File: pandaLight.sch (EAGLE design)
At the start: 161 parts, among them J1 PJ-037A, U1 MIC23450AAAYML, U10 AS4C128M16D3, U11 PMOD-2X6, U12 PMOD-2X6, U13 PLR135-T10, U14 PLT133-T10W, U15 PLR135-T10, U16 TP10SQ, U17 TP10SQ, U18 PAN1322, U2 6SLX45CSG324, U3 TPD4S014SON, U4 FT2232HL, U5 93LC46BT-I/OT, U6 TPD12S016PWR, U7 TPD12S016PWR, U8 N25Q128AF8, U9 TPD12S016PWR, X1 USBUB-S, X2 HDMI_RECEPTICAL_A, X3 HDMI_RECEPTICAL_A, X4 HDMI_RECEPTICAL_A, Y1 403, Y2 20Mhz

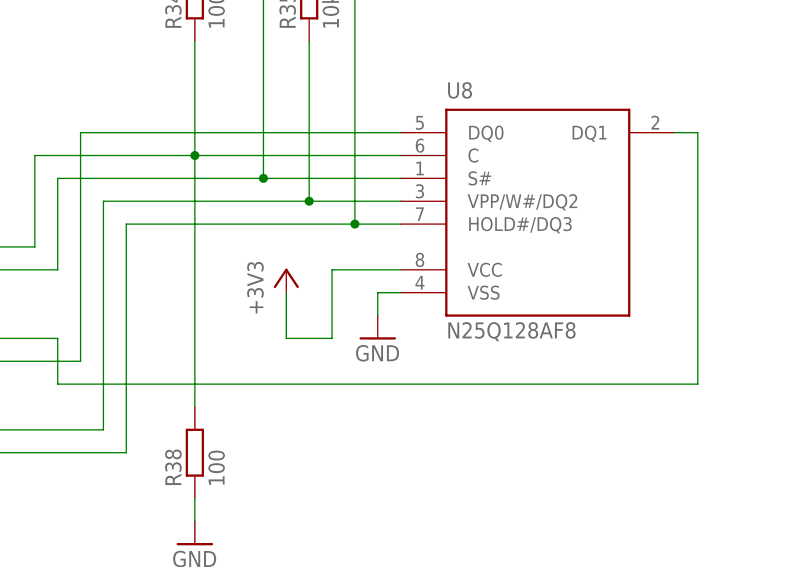
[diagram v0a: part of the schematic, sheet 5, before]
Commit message: First routing of the serial flash; Placed some more bypass capacitors
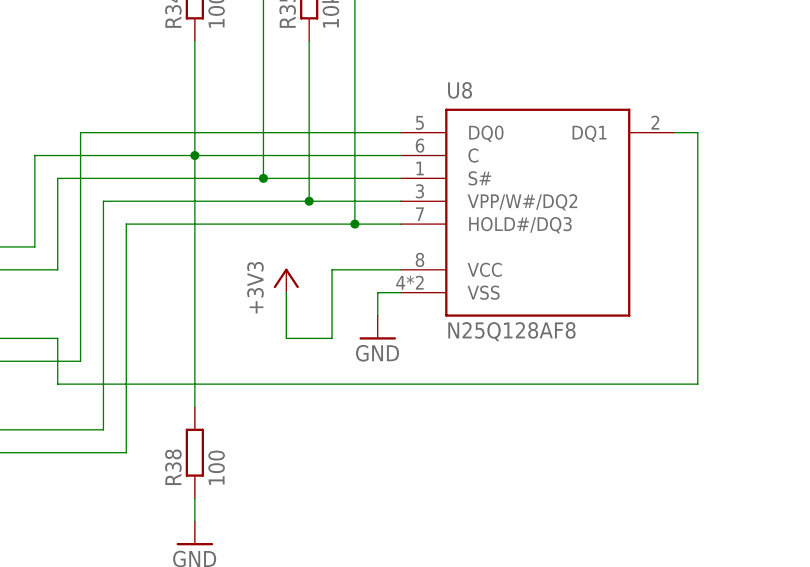
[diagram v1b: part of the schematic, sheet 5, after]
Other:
- moved on the sheet: U8

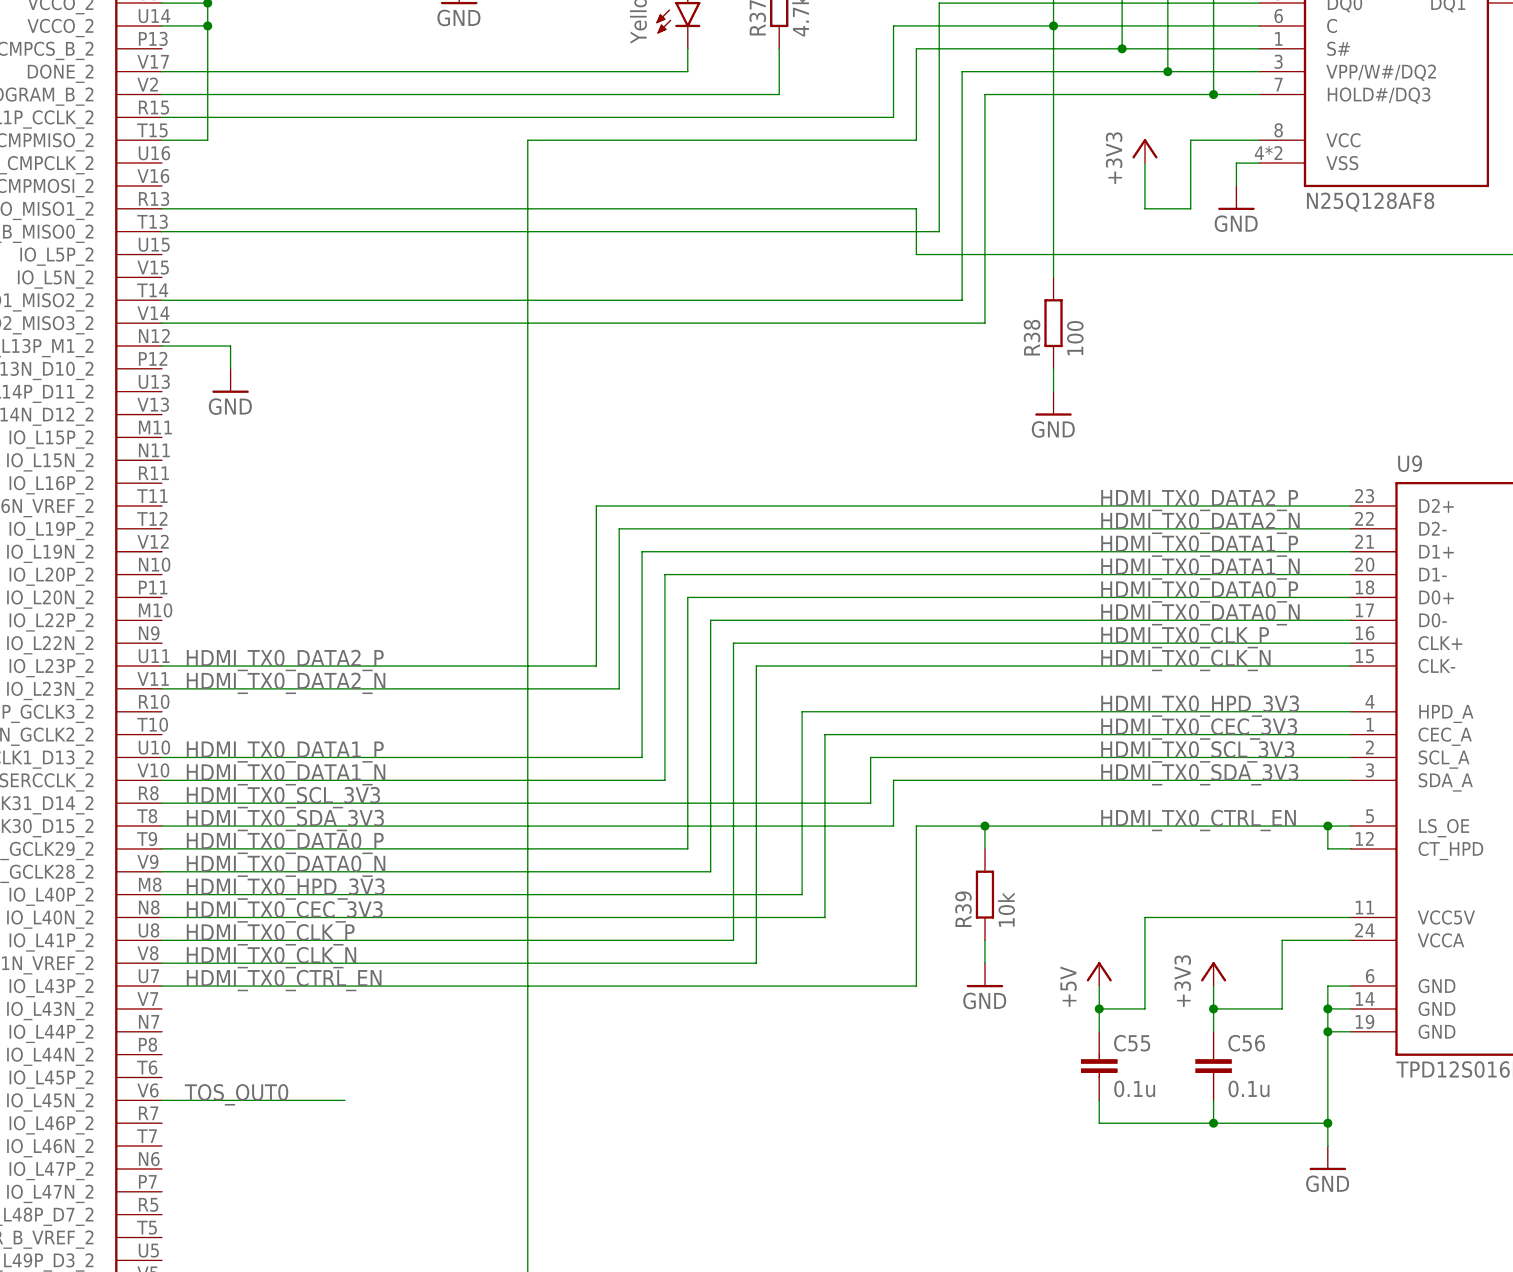
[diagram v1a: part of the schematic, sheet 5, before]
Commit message: Routed HDMI_TX0; Placed the PMODs to the board's bottom left edge
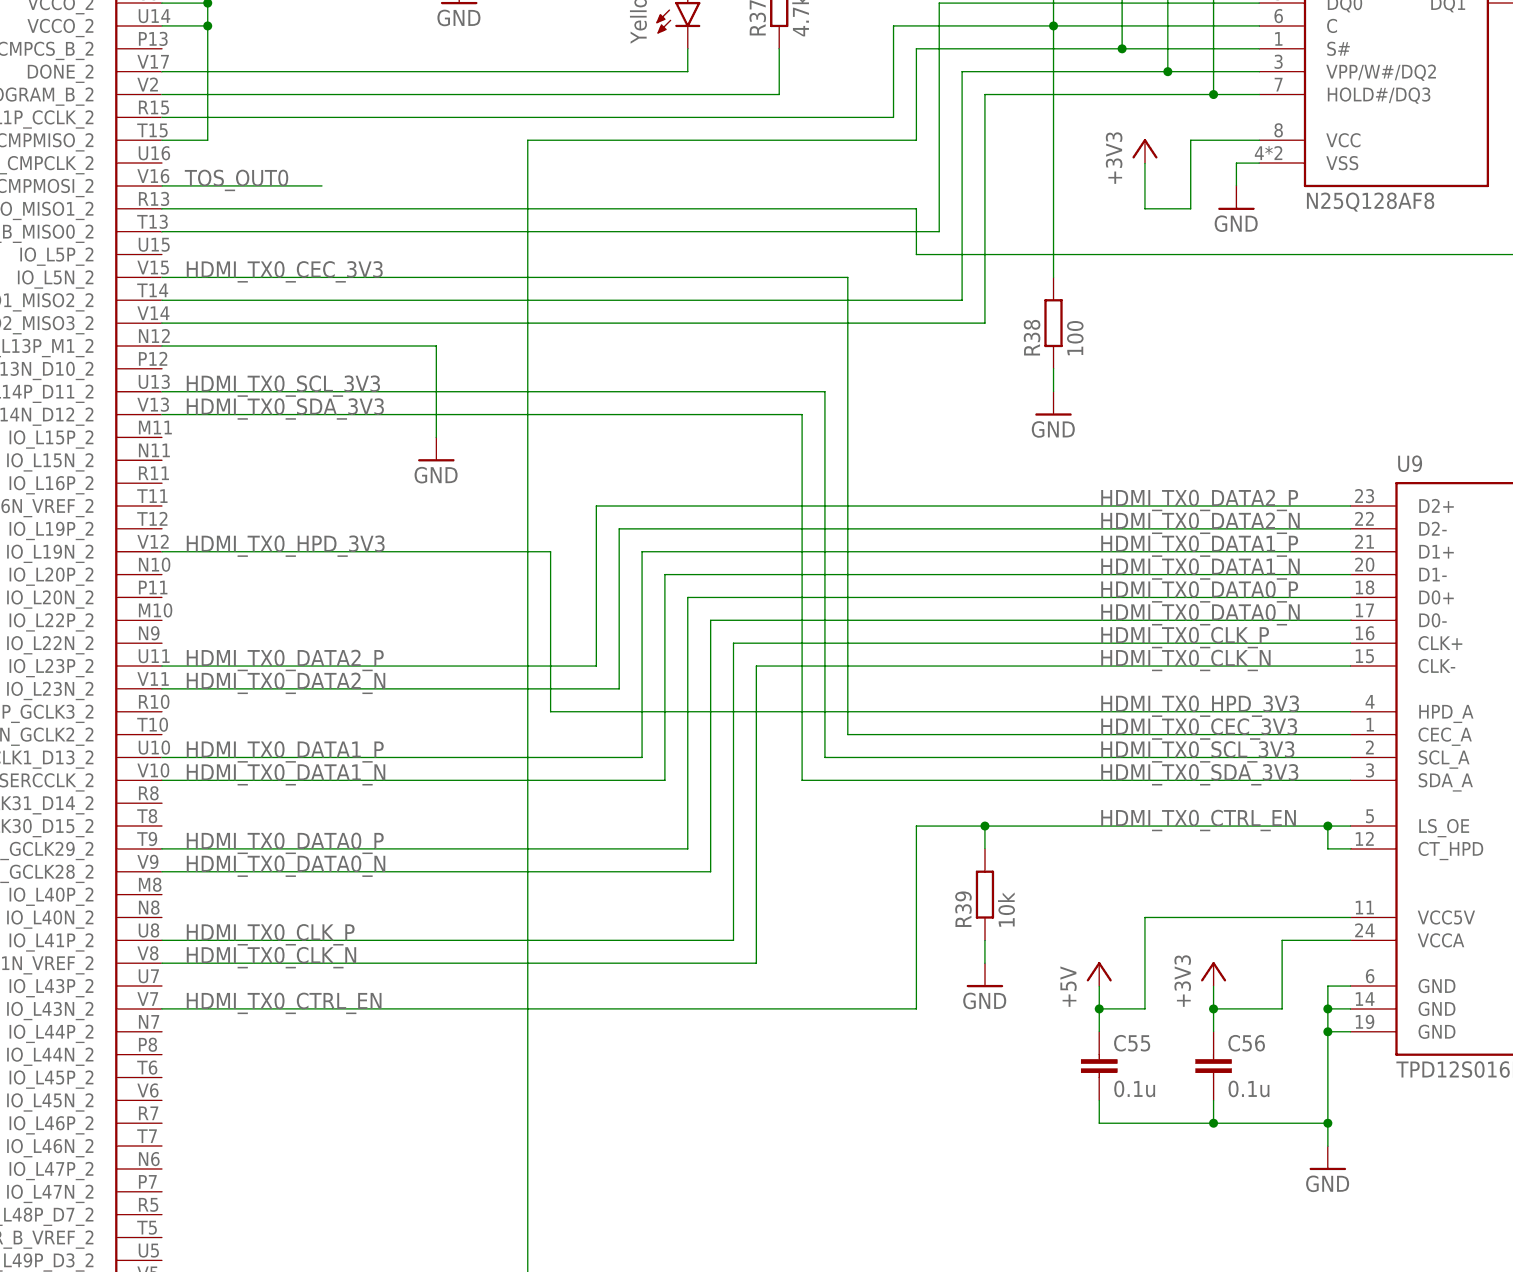
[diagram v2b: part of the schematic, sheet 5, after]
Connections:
- net HDMI_TX0_CEC_3V3: now also U2B2.IO_L5N_2; no longer U2B2.IO_L40N_2
- net HDMI_TX0_CTRL_EN: now also U2B2.IO_L43N_2; no longer U2B2.IO_L43P_2
- net HDMI_TX0_HPD_3V3: now also U2B2.IO_L19N_2; no longer U2B2.IO_L40P_2
- net HDMI_TX0_SCL_3V3: now also U2B2.IO_L14P_D11_2; no longer U2B2.IO_L31P_GCLK31_D14_2
- net HDMI_TX0_SDA_3V3: now also U2B2.IO_L14N_D12_2; no longer U2B2.IO_L31N_GCLK30_D15_2
- net TOS_OUT0: now also U2B2.IO_L2N_CMPMOSI_2; no longer U2B2.IO_L45N_2
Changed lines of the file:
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@@
 <attribute name="PARTNO" x="109.22" y="172.72" size="1.778" layer="96" display="off"/>
 </instance>
-<instance part="GND40" gate="1" x="48.26" y="129.54"/>
+<instance part="GND40" gate="1" x="71.12" y="121.92"/>
 <instance part="LED2" gate="G$1" x="99.06" y="172.72" rot="R270">
 <attribute name="PARTNO" x="99.06" y="172.72" size="1.778" layer="96" display="off"/>
@@
 <segment>
 <pinref part="GND40" gate="1" pin="GND"/>
-<wire x1="48.26" y1="134.62" x2="48.26" y2="132.08" width="0.1524" layer="91"/>
+<wire x1="71.12" y1="134.62" x2="71.12" y2="124.46" width="0.1524" layer="91"/>
 <pinref part="U2" gate="B2" pin="IO_L13P_M1_2"/>
-<wire x1="40.64" y1="134.62" x2="48.26" y2="134.62" width="0.1524" layer="91"/>
+<wire x1="40.64" y1="134.62" x2="71.12" y2="134.62" width="0.1524" layer="91"/>
 </segment>
 <segment>
@@
 <pinref part="U9" gate="G$1" pin="HPD_A"/>
 <label x="144.78" y="93.98" size="1.778" layer="95"/>
-<pinref part="U2" gate="B2" pin="IO_L40P_2"/>
-<wire x1="172.72" y1="93.98" x2="111.76" y2="93.98" width="0.1524" layer="91"/>
-<wire x1="111.76" y1="93.98" x2="111.76" y2="73.66" width="0.1524" layer="91"/>
-<wire x1="111.76" y1="73.66" x2="40.64" y2="73.66" width="0.1524" layer="91"/>
-<label x="43.18" y="73.66" size="1.778" layer="95"/>
+<pinref part="U2" gate="B2" pin="IO_L19N_2"/>
+<wire x1="172.72" y1="93.98" x2="83.82" y2="93.98" width="0.1524" layer="91"/>
+<wire x1="83.82" y1="93.98" x2="83.82" y2="111.76" width="0.1524" layer="91"/>
+<wire x1="83.82" y1="111.76" x2="40.64" y2="111.76" width="0.1524" layer="91"/>
+<label x="43.18" y="111.76" size="1.778" layer="95"/>
 </segment>
 </net>
@@
 <pinref part="U9" gate="G$1" pin="CEC_A"/>
 <label x="144.78" y="91.44" size="1.778" layer="95"/>
-<pinref part="U2" gate="B2" pin="IO_L40N_2"/>
-<wire x1="172.72" y1="91.44" x2="114.3" y2="91.44" width="0.1524" layer="91"/>
-<wire x1="114.3" y1="91.44" x2="114.3" y2="71.12" width="0.1524" layer="91"/>
-<wire x1="114.3" y1="71.12" x2="40.64" y2="71.12" width="0.1524" layer="91"/>
-<label x="43.18" y="71.12" size="1.778" layer="95"/>
+<pinref part="U2" gate="B2" pin="IO_L5N_2"/>
+<wire x1="172.72" y1="91.44" x2="116.84" y2="91.44" width="0.1524" layer="91"/>
+<wire x1="116.84" y1="91.44" x2="116.84" y2="142.24" width="0.1524" layer="91"/>
+<wire x1="116.84" y1="142.24" x2="40.64" y2="142.24" width="0.1524" layer="91"/>
+<label x="43.18" y="142.24" size="1.778" layer="95"/>
 </segment>
 </net>
@@
 <segment>
 <pinref part="U9" gate="G$1" pin="SCL_A"/>
-<wire x1="172.72" y1="88.9" x2="119.38" y2="88.9" width="0.1524" layer="91"/>
+<wire x1="172.72" y1="88.9" x2="114.3" y2="88.9" width="0.1524" layer="91"/>
 <label x="144.78" y="88.9" size="1.778" layer="95"/>
-<wire x1="119.38" y1="88.9" x2="119.38" y2="83.82" width="0.1524" layer="91"/>
-<pinref part="U2" gate="B2" pin="IO_L31P_GCLK31_D14_2"/>
-<wire x1="119.38" y1="83.82" x2="40.64" y2="83.82" width="0.1524" layer="91"/>
-<label x="43.18" y="83.82" size="1.778" layer="95"/>
+<wire x1="114.3" y1="88.9" x2="114.3" y2="129.54" width="0.1524" layer="91"/>
+<pinref part="U2" gate="B2" pin="IO_L14P_D11_2"/>
+<wire x1="114.3" y1="129.54" x2="40.64" y2="129.54" width="0.1524" layer="91"/>
+<label x="43.18" y="129.54" size="1.778" layer="95"/>
 </segment>
 </net>
@@
 <segment>
 <pinref part="U9" gate="G$1" pin="SDA_A"/>
-<wire x1="172.72" y1="86.36" x2="121.92" y2="86.36" width="0.1524" layer="91"/>
+<wire x1="172.72" y1="86.36" x2="111.76" y2="86.36" width="0.1524" layer="91"/>
 <label x="144.78" y="86.36" size="1.778" layer="95"/>
-<wire x1="121.92" y1="86.36" x2="121.92" y2="81.28" width="0.1524" layer="91"/>
-<pinref part="U2" gate="B2" pin="IO_L31N_GCLK30_D15_2"/>
-<wire x1="40.64" y1="81.28" x2="121.92" y2="81.28" width="0.1524" layer="91"/>
-<label x="43.18" y="81.28" size="1.778" layer="95"/>
+<wire x1="111.76" y1="86.36" x2="111.76" y2="127" width="0.1524" layer="91"/>
+<pinref part="U2" gate="B2" pin="IO_L14N_D12_2"/>
+<wire x1="40.64" y1="127" x2="111.76" y2="127" width="0.1524" layer="91"/>
+<label x="43.18" y="127" size="1.778" layer="95"/>
 </segment>
 </net>
@@
 <junction x="132.08" y="81.28"/>
 <wire x1="132.08" y1="81.28" x2="124.46" y2="81.28" width="0.1524" layer="91"/>
-<wire x1="124.46" y1="81.28" x2="124.46" y2="63.5" width="0.1524" layer="91"/>
-<pinref part="U2" gate="B2" pin="IO_L43P_2"/>
-<wire x1="40.64" y1="63.5" x2="124.46" y2="63.5" width="0.1524" layer="91"/>
-<label x="43.18" y="63.5" size="1.778" layer="95"/>
+<wire x1="124.46" y1="81.28" x2="124.46" y2="60.96" width="0.1524" layer="91"/>
+<pinref part="U2" gate="B2" pin="IO_L43N_2"/>
+<wire x1="40.64" y1="60.96" x2="124.46" y2="60.96" width="0.1524" layer="91"/>
+<label x="43.18" y="60.96" size="1.778" layer="95"/>
 </segment>
 </net>
@@
 <net name="TOS_OUT0" class="0">
 <segment>
-<pinref part="U2" gate="B2" pin="IO_L45N_2"/>
-<wire x1="40.64" y1="50.8" x2="60.96" y2="50.8" width="0.1524" layer="91"/>
-<label x="43.18" y="50.8" size="1.778" layer="95"/>
-</segment>
-</net>
+<pinref part="U2" gate="B2" pin="IO_L2N_CMPMOSI_2"/>
+<wire x1="40.64" y1="152.4" x2="58.42" y2="152.4" width="0.1524" layer="91"/>
+<label x="43.18" y="152.4" size="1.778" layer="95"/>
+</segment>
+</net>

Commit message: Switched the 1*8 resistor networks with 2*4 ones; Moved the HDMI_RX0 nets to the top layer
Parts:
- removed C72: 0.1u, pandaLight:CAPACITOR0402
- removed RN1, RN2: MNR18, pandaLight:MNR18
- added C9: 100u, pandaLight:CAPACITOR1206
- added U19: PLR135-T10, pandaLight:PLR135-T10
- added U20, U21: TP10SQ, pandaLight:TP10SQ
- added U22: PAN1322, pandaLight:PAN1322
- C10: value 100u -> 4.7u; device pandaLight:CAPACITOR1206 -> pandaLight:CAPACITOR0603; PARTNO CL31A107MQHNNNE -> C0603C475K9PACTU
- C11, C38, C45, C51, C57: value 4.7u -> 0.47u; device pandaLight:CAPACITOR0603 -> pandaLight:CAPACITOR0402; PARTNO C0603C475K9PACTU -> C1005X5R0J474K050BB
- C14, C40, C47, C53: value 0.47u -> 0.1u; PARTNO C1005X5R0J474K050BB -> CL05B104KP5NNNC
- C17, C24, C28, C30, C32, C37, C44, C50, C56: value 0.1u -> 4.7u; device pandaLight:CAPACITOR0402 -> pandaLight:CAPACITOR0603; PARTNO CL05B104KP5NNNC -> C0603C475K9PACTU
- C20, C25, C29, C31: value 4.7u -> 0.1u; device pandaLight:CAPACITOR0603 -> pandaLight:CAPACITOR0402; PARTNO C0603C475K9PACTU -> CL05B104KP5NNNC
- C33: value 4.7u -> 100u; device pandaLight:CAPACITOR0603 -> pandaLight:CAPACITOR1206; PARTNO C0603C475K9PACTU -> CL31A107MQHNNNE
- C34: value 100u -> 27p; device pandaLight:CAPACITOR1206 -> pandaLight:CAPACITOR0402; PARTNO CL31A107MQHNNNE -> CL05C270JB5NNNC
- C36: value 27p -> 0.1u; PARTNO CL05C270JB5NNNC -> CL05B104KP5NNNC
- C59: value 0.47u -> 1u; PARTNO C1005X5R0J474K050BB -> C1005X5R0J105M050BB
- C61: value 1u -> 0.1u; PARTNO C1005X5R0J105M050BB -> CL05B104KP5NNNC
- U10: value AS4C128M16D3 -> 51; device pandaLight:AS4C128M16D3 -> pandaLight:741C083; PARTNO AS4C128M16D3-12BCN -> 741C083510JP
- U11: value PMOD-2X6 -> TPD12S016PWR; device pandaLight:PMOD-2X6 -> pandaLight:TPD12S016PWR; PARTNO PPTC062LJBN-RC -> TPD12S016PWR
- U12: value PMOD-2X6 -> N25Q128AF8; device pandaLight:PMOD-2X6 -> pandaLight:N25Q128AF8; PARTNO PPTC062LJBN-RC -> N25Q128A13EF840E
- U13: value PLR135-T10 -> TPD12S016PWR; device pandaLight:PLR135-T10 -> pandaLight:TPD12S016PWR; PARTNO PLR135/T10 -> TPD12S016PWR
- U14: value PLT133-T10W -> AS4C128M16D3; device pandaLight:PLT133-T10W -> pandaLight:AS4C128M16D3; PARTNO PLT133/T10W -> AS4C128M16D3-12BCN
- U15: value PLR135-T10 -> PMOD-2X6; device pandaLight:PLR135-T10 -> pandaLight:PMOD-2X6; PARTNO PLR135/T10 -> PPTC062LJBN-RC
- U16: value TP10SQ -> PMOD-2X6; device pandaLight:TP10SQ -> pandaLight:PMOD-2X6; BOM EXCLUDE -> (none); PARTNO * -> PPTC062LJBN-RC
- U17: value TP10SQ -> PLR135-T10; device pandaLight:TP10SQ -> pandaLight:PLR135-T10; BOM EXCLUDE -> (none); PARTNO * -> PLR135/T10
- U18: value PAN1322 -> PLT133-T10W; device pandaLight:PAN1322 -> pandaLight:PLT133-T10W; PARTNO ENW-89841A3KF -> PLT133/T10W
- U6, U7, U9: value TPD12S016PWR -> 51; device pandaLight:TPD12S016PWR -> pandaLight:741C083; PARTNO TPD12S016PWR -> 741C083510JP
- U8: value N25Q128AF8 -> TPD12S016PWR; device pandaLight:N25Q128AF8 -> pandaLight:TPD12S016PWR; PARTNO N25Q128A13EF840E -> TPD12S016PWR
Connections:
- net +1V2: now also C19.1; no longer C20.1
- net +1V5: now also C18.1, C56.1, U14.VDD@B2, U14.VDD@D9, U14.VDD@G7, U14.VDD@K2, U14.VDD@K8, U14.VDD@N1, U14.VDD@N9, U14.VDD@R1, U14.VDD@R9, U14.VDDQ@A1, U14.VDDQ@A8, U14.VDDQ@C1, U14.VDDQ@C9, U14.VDDQ@D2, U14.VDDQ@E9, U14.VDDQ@F1, U14.VDDQ@H2, U14.VDDQ@H9; no longer C19.1, C64.1, U10.VDD@B2, U10.VDD@D9, U10.VDD@G7, U10.VDD@K2, U10.VDD@K8, U10.VDD@N1, U10.VDD@N9, U10.VDD@R1, U10.VDD@R9, U10.VDDQ@A1, U10.VDDQ@A8, U10.VDDQ@C1, U10.VDDQ@C9, U10.VDDQ@D2, U10.VDDQ@E9, U10.VDDQ@F1, U10.VDDQ@H2, U10.VDDQ@H9
- net +1V5_VREF: now also C63.2, C64.1, U14.VREFCA, U14.VREFDQ; no longer C64.2, C67.1, U10.VREFCA, U10.VREFDQ
- net +1V8: now also C24.1; no longer C28.1
- net +3V3: now also C17.1, C20.1, C32.1, C36.1, C42.1, C49.1, C55.1, C68.1, C70.1, C9.1, U10.13, U10.15, U10.16, U10.C3, U11.VCCA, U12.VCC, U13.VCCA, U18.VCC, U22.ONOFF, U22.VDD1, U22.VDDUART, U22.VSUPPLY@A4, U22.VSUPPLY@A5, U22.VSUPPLY@A6, U6.13, U6.15, U6.16, U6.C3, U7.13, U7.15, U7.16, U7.C3, U8.VCCA, U9.13, U9.15, U9.16, U9.C3; no longer C14.1, C18.1, C24.1, C33.1, C40.1, C47.1, C53.1, C56.1, C69.1, C72.1, RN1.10, RN1.11, RN1.12, RN1.13, RN1.15, RN1.16, RN1.9, RN1.C3, RN2.10, RN2.11, RN2.12, RN2.13, RN2.15, RN2.16, RN2.9, RN2.C3, U14.VCC, U18.ONOFF, U18.VDD1, U18.VDDUART, U18.VSUPPLY@A4, U18.VSUPPLY@A5, U18.VSUPPLY@A6, U6.VCCA, U7.VCCA, U8.VCC, U9.VCCA
- net +5V: now also C41.1, C48.1, C54.1, U11.VCC5V, U13.VCC5V, U8.VCC5V; no longer C42.1, C49.1, C55.1, U6.VCC5V, U7.VCC5V, U9.VCC5V
- net BT_CTS: now also U22.P0.7_UARTCTS; no longer U18.P0.7_UARTCTS
- net BT_RESET#: now also U22.RESET#; no longer U18.RESET#
- net BT_RTS: now also U22.P0.6_UARTRTS; no longer U18.P0.6_UARTRTS
- net BT_RX: now also U22.P0.5_UARTRXD; no longer U18.P0.5_UARTRXD
- net BT_TX: now also U22.P0.4_UARTTXD; no longer U18.P0.4_UARTTXD
- net BT_WAKE: now also U22.P0.14_LPMIN; no longer U18.P0.14_LPMIN
- net DDR3_A0: now also U14.A0; no longer U10.A0
- net DDR3_A1: now also U14.A1; no longer U10.A1
- net DDR3_A10: now also U14.A10/AP; no longer U10.A10/AP
- net DDR3_A11: now also U14.A11; no longer U10.A11
- net DDR3_A12: now also U14.A12/BC#; no longer U10.A12/BC#
- net DDR3_A2: now also U14.A2; no longer U10.A2
- net DDR3_A3: now also U14.A3; no longer U10.A3
- net DDR3_A4: now also U14.A4; no longer U10.A4
- net DDR3_A5: now also U14.A5; no longer U10.A5
- net DDR3_A6: now also U14.A6; no longer U10.A6
- net DDR3_A7: now also U14.A7; no longer U10.A7
- net DDR3_A8: now also U14.A8; no longer U10.A8
- net DDR3_A9: now also U14.A9; no longer U10.A9
- net DDR3_BA0: now also U14.BA0; no longer U10.BA0
- net DDR3_BA1: now also U14.BA1; no longer U10.BA1
- net DDR3_BA2: now also U14.BA2; no longer U10.BA2
- net DDR3_CAS#: now also U14.CAS#; no longer U10.CAS#
- net DDR3_CK: now also U14.CK; no longer U10.CK
- net DDR3_CK#: now also U14.CK#; no longer U10.CK#
- net DDR3_CKE: now also U14.CKE; no longer U10.CKE
- net DDR3_DQ0: now also U14.DQ0; no longer U10.DQ0
- net DDR3_DQ1: now also U14.DQ1; no longer U10.DQ1
- net DDR3_DQ10: now also U14.DQ10; no longer U10.DQ10
- net DDR3_DQ11: now also U14.DQ11; no longer U10.DQ11
- net DDR3_DQ12: now also U14.DQ12; no longer U10.DQ12
- net DDR3_DQ13: now also U14.DQ13; no longer U10.DQ13
- net DDR3_DQ14: now also U14.DQ14; no longer U10.DQ14
- net DDR3_DQ15: now also U14.DQ15; no longer U10.DQ15
- net DDR3_DQ2: now also U14.DQ2; no longer U10.DQ2
- net DDR3_DQ3: now also U14.DQ3; no longer U10.DQ3
- net DDR3_DQ4: now also U14.DQ4; no longer U10.DQ4
- net DDR3_DQ5: now also U14.DQ5; no longer U10.DQ5
- net DDR3_DQ6: now also U14.DQ6; no longer U10.DQ6
- net DDR3_DQ7: now also U14.DQ7; no longer U10.DQ7
- net DDR3_DQ8: now also U14.DQ8; no longer U10.DQ8
- net DDR3_DQ9: now also U14.DQ9; no longer U10.DQ9
- net DDR3_LDM: now also U14.LDM; no longer U10.LDM
- net DDR3_LDQS: now also U14.LDQS; no longer U10.LDQS
- net DDR3_LDQS#: now also U14.LDQS#; no longer U10.LDQS#
- net DDR3_ODT: now also U14.ODT; no longer U10.ODT
- net DDR3_RAS#: now also U14.RAS#; no longer U10.RAS#
- net DDR3_RESET#: now also U14.RESET#; no longer U10.RESET#
- net DDR3_UDM: now also U14.UDM; no longer U10.UDM
- net DDR3_UDQS: now also U14.UDQS; no longer U10.UDQS
- net DDR3_UDQS#: now also U14.UDQS#; no longer U10.UDQS#
- net DDR3_WE#: now also U14.WE#; no longer U10.WE#
- net GND: now also C64.2, C9.2, U11.GND@0, U11.GND@1, U11.GND@2, U12.VSS, U13.GND@0, U13.GND@1, U13.GND@2, U14.CS#, U14.VSS@A9, U14.VSS@B3, U14.VSS@E1, U14.VSS@G8, U14.VSS@J2, U14.VSS@J8, U14.VSS@M1, U14.VSS@M9, U14.VSS@P1, U14.VSS@P9, U14.VSS@T1, U14.VSS@T9, U14.VSSQ@B1, U14.VSSQ@B9, U14.VSSQ@D1, U14.VSSQ@D8, U14.VSSQ@E2, U14.VSSQ@E8, U14.VSSQ@F9, U14.VSSQ@G1, U14.VSSQ@G9, U15.11, U15.5, U16.11, U16.5, U17.GND, U18.GND, U19.GND, U22.VSS@A1, U22.VSS@A11, U22.VSS@A12, U22.VSS@A7, U22.VSS@A9, U22.VSS@C8, U22.VSS@C9, U22.VSS@D7, U22.VSS@D8, U22.VSS@E8, U22.VSS@E9, U22.VSS@F1, U22.VSS@F11, U22.VSS@F12, U22.VSS@F9, U8.GND@0, U8.GND@1, U8.GND@2; no longer C63.2, C72.2, U10.CS#, U10.VSS@A9, U10.VSS@B3, U10.VSS@E1, U10.VSS@G8, U10.VSS@J2, U10.VSS@J8, U10.VSS@M1, U10.VSS@M9, U10.VSS@P1, U10.VSS@P9, U10.VSS@T1, U10.VSS@T9, U10.VSSQ@B1, U10.VSSQ@B9, U10.VSSQ@D1, U10.VSSQ@D8, U10.VSSQ@E2, U10.VSSQ@E8, U10.VSSQ@F9, U10.VSSQ@G1, U10.VSSQ@G9, U11.11, U11.5, U12.11, U12.5, U13.GND, U14.GND, U15.GND, U18.VSS@A1, U18.VSS@A11, U18.VSS@A12, U18.VSS@A7, U18.VSS@A9, U18.VSS@C8, U18.VSS@C9, U18.VSS@D7, U18.VSS@D8, U18.VSS@E8, U18.VSS@E9, U18.VSS@F1, U18.VSS@F11, U18.VSS@F12, U18.VSS@F9, U6.GND@0, U6.GND@1, U6.GND@2, U7.GND@0, U7.GND@1, U7.GND@2, U8.VSS, U9.GND@0, U9.GND@1, U9.GND@2
- net HDMI_RX0_5V: now also C40.1, U8.5V_OUT; no longer C41.1, U6.5V_OUT
- net HDMI_RX0_CEC: now also U8.CEC_B; no longer U6.CEC_B
- net HDMI_RX0_CEC_3V3: now also U8.CEC_A; no longer U6.CEC_A
- net HDMI_RX0_CLK_N: now also U7.1, U8.CLK-; no longer RN1.8, U6.CLK-
- net HDMI_RX0_CLK_P: now also U7.2, U8.CLK+; no longer RN1.7, U6.CLK+
- net HDMI_RX0_CTRL_EN: now also U8.CT_HPD, U8.LS_OE; no longer U6.CT_HPD, U6.LS_OE
- net HDMI_RX0_DATA0_N: now also U7.3, U8.D0-; no longer RN1.6, U6.D0-
- net HDMI_RX0_DATA0_P: now also U7.4, U8.D0+; no longer RN1.5, U6.D0+
- net HDMI_RX0_DATA1_N: now also U6.1, U8.D1-; no longer RN1.4, U6.D1-
- net HDMI_RX0_DATA1_P: now also U6.2, U8.D1+; no longer RN1.3, U6.D1+
- net HDMI_RX0_DATA2_N: now also U6.3, U8.D2-; no longer RN1.2, U6.D2-
- net HDMI_RX0_DATA2_P: now also U6.4, U8.D2+; no longer RN1.1, U6.D2+
- net HDMI_RX0_SCL_3V3: now also U8.SCL_A; no longer U6.SCL_A
- net HDMI_RX0_SCL_5V: now also U8.SCL_B; no longer U6.SCL_B
- net HDMI_RX0_SDA_3V3: now also U8.SDA_A; no longer U6.SDA_A
- net HDMI_RX0_SDA_5V: now also U8.SDA_B; no longer U6.SDA_B
- net HDMI_RX1_5V: now also C47.1, U11.5V_OUT; no longer C48.1, U7.5V_OUT
- net HDMI_RX1_CEC: now also U11.CEC_B; no longer U7.CEC_B
- net HDMI_RX1_CEC_3V3: now also U11.CEC_A; no longer U7.CEC_A
- net HDMI_RX1_CLK_N: now also U10.1, U11.CLK-; no longer RN2.8, U7.CLK-
- net HDMI_RX1_CLK_P: now also U10.2, U11.CLK+; no longer RN2.7, U7.CLK+
- net HDMI_RX1_CTRL_EN: now also U11.CT_HPD, U11.LS_OE; no longer U7.CT_HPD, U7.LS_OE
- net HDMI_RX1_DATA0_N: now also U10.3, U11.D0-; no longer RN2.6, U7.D0-
- net HDMI_RX1_DATA0_P: now also U10.4, U11.D0+; no longer RN2.5, U7.D0+
- net HDMI_RX1_DATA1_N: now also U11.D1-, U9.1; no longer RN2.4, U7.D1-
- net HDMI_RX1_DATA1_P: now also U11.D1+, U9.2; no longer RN2.3, U7.D1+
- net HDMI_RX1_DATA2_N: now also U11.D2-, U9.3; no longer RN2.2, U7.D2-
- net HDMI_RX1_DATA2_P: now also U11.D2+, U9.4; no longer RN2.1, U7.D2+
- net HDMI_RX1_SCL_3V3: now also U11.SCL_A; no longer U7.SCL_A
- net HDMI_RX1_SCL_5V: now also U11.SCL_B; no longer U7.SCL_B
- net HDMI_RX1_SDA_3V3: now also U11.SDA_A; no longer U7.SDA_A
- net HDMI_RX1_SDA_5V: now also U11.SDA_B; no longer U7.SDA_B
- net HDMI_TX0_5V: now also C53.1, U13.5V_OUT; no longer C54.1, U9.5V_OUT
- net HDMI_TX0_CEC: now also U13.CEC_B; no longer U9.CEC_B
- net HDMI_TX0_CEC_3V3: now also U13.CEC_A; no longer U9.CEC_A
- net HDMI_TX0_CLK_N: now also U13.CLK-; no longer U9.CLK-
- net HDMI_TX0_CLK_P: now also U13.CLK+; no longer U9.CLK+
- net HDMI_TX0_CTRL_EN: now also U13.CT_HPD, U13.LS_OE; no longer U9.CT_HPD, U9.LS_OE
- net HDMI_TX0_DATA0_N: now also U13.D0-; no longer U9.D0-
- net HDMI_TX0_DATA0_P: now also U13.D0+; no longer U9.D0+
- net HDMI_TX0_DATA1_N: now also U13.D1-; no longer U9.D1-
- net HDMI_TX0_DATA1_P: now also U13.D1+; no longer U9.D1+
- net HDMI_TX0_DATA2_N: now also U13.D2-; no longer U9.D2-
- net HDMI_TX0_DATA2_P: now also U13.D2+; no longer U9.D2+
- net HDMI_TX0_HPD_3V3: now also U13.HPD_A; no longer U9.HPD_A
- net HDMI_TX0_HPD_5V: now also U13.HPD_B; no longer U9.HPD_B
- net HDMI_TX0_SCL_3V3: now also U13.SCL_A; no longer U9.SCL_A
- net HDMI_TX0_SCL_5V: now also U13.SCL_B; no longer U9.SCL_B
- net HDMI_TX0_SDA_3V3: now also U13.SDA_A; no longer U9.SDA_A
- net HDMI_TX0_SDA_5V: now also U13.SDA_B; no longer U9.SDA_B
- net N$1: now also C35.1; no longer C36.1
- net N$15: now also C16.1; no longer C17.1
- net N$19: now also U21.TP, U22.P0.12_SDA0; no longer U17.TP, U18.P0.12_SDA0
- net N$28: now also C30.1; no longer C32.1
- net N$29: now also U20.TP, U22.P0.13_SCL0; no longer U16.TP, U18.P0.13_SCL0
- net N$3: now also U14.ZQ; no longer U10.ZQ
- net N$30: now also C15.1; no longer C16.1
- net N$31: now also C28.1; no longer C30.1
- net N$36: now also C67.1, U17.VCC; no longer C68.1, U13.VCC
- net N$4: now also C69.1, U19.VCC; no longer C70.1, U15.VCC
- net N$40: now also U12.DQ0; no longer U8.DQ0
- net N$41: now also U12.S#; no longer U8.S#
- net N$42: now also U12.C; no longer U8.C
- net N$43: now also U12.DQ1; no longer U8.DQ1
- net N$44: now also U12.VPP/W#/DQ2; no longer U8.VPP/W#/DQ2
- net N$45: now also C33.1; no longer C34.1
- net N$46: now also U12.HOLD#/DQ3; no longer U8.HOLD#/DQ3
- net N$48: now also C14.1; no longer C15.1
- net N$49: now also U16.12, U16.6; no longer U12.12, U12.6
- net N$5: now also C34.1; no longer C35.1
- net N$51: now also U15.12, U15.6; no longer U11.12, U11.6
- net PMOD0_0: now also U15.1; no longer U11.1
- net PMOD0_1: now also U15.2; no longer U11.2
- net PMOD0_2: now also U15.3; no longer U11.3
- net PMOD0_3: now also U15.4; no longer U11.4
- net PMOD1_0: now also U15.7; no longer U11.7
- net PMOD1_1: now also U15.8; no longer U11.8
- net PMOD1_2: now also U15.9; no longer U11.9
- net PMOD1_3: now also U15.10; no longer U11.10
- net PMOD2_0: now also U16.1; no longer U12.1
- net PMOD2_1: now also U16.2; no longer U12.2
- net PMOD2_2: now also U16.3; no longer U12.3
- net PMOD2_3: now also U16.4; no longer U12.4
- net PMOD3_0: now also U16.7; no longer U12.7
- net PMOD3_1: now also U16.8; no longer U12.8
- net PMOD3_2: now also U16.9; no longer U12.9
- net PMOD3_3: now also U16.10; no longer U12.10
- net TOS_IN0: now also U17.VOUT; no longer U13.VOUT
- net TOS_IN1: now also U19.VOUT; no longer U15.VOUT
- net TOS_OUT0: now also U18.VIN; no longer U14.VIN
